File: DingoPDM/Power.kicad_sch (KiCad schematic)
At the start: 29 parts, among them J5 SHORT, SW2 AlwaysOn, U18 LD1117S33CTR, U22 VXO780x-500-M, U23 ISP752R

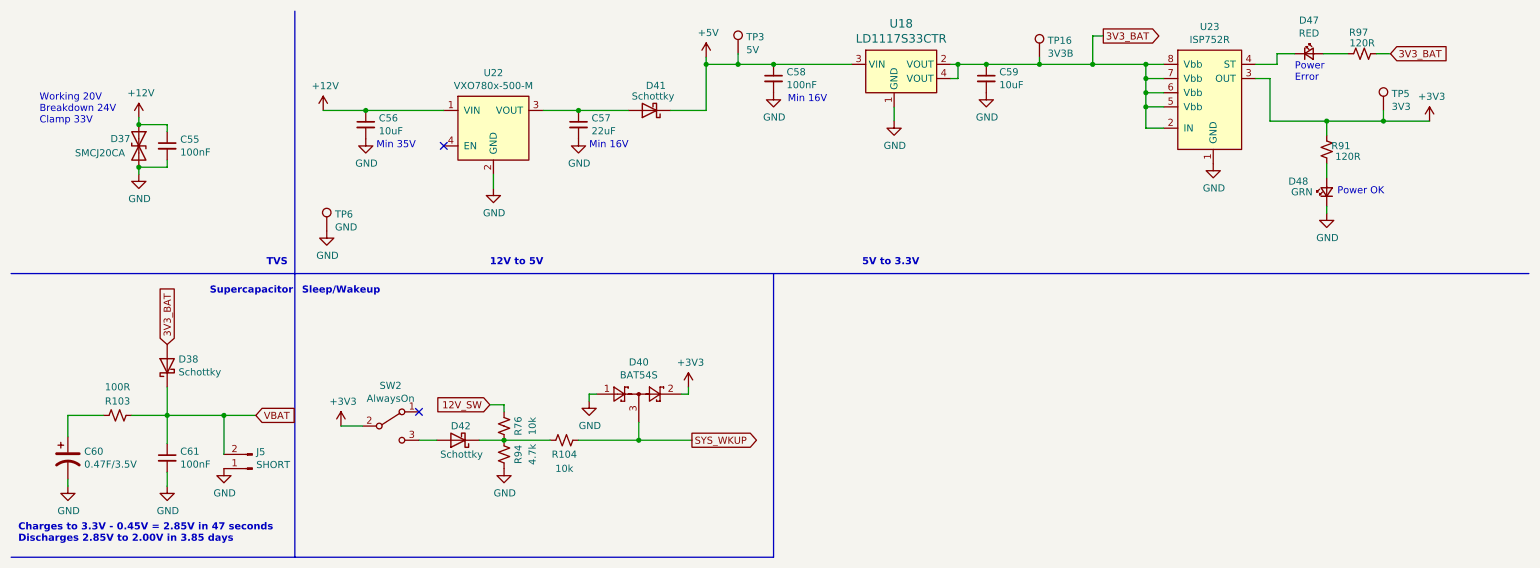
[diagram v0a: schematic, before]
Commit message: Swapped to AMPSEAL 14 pins
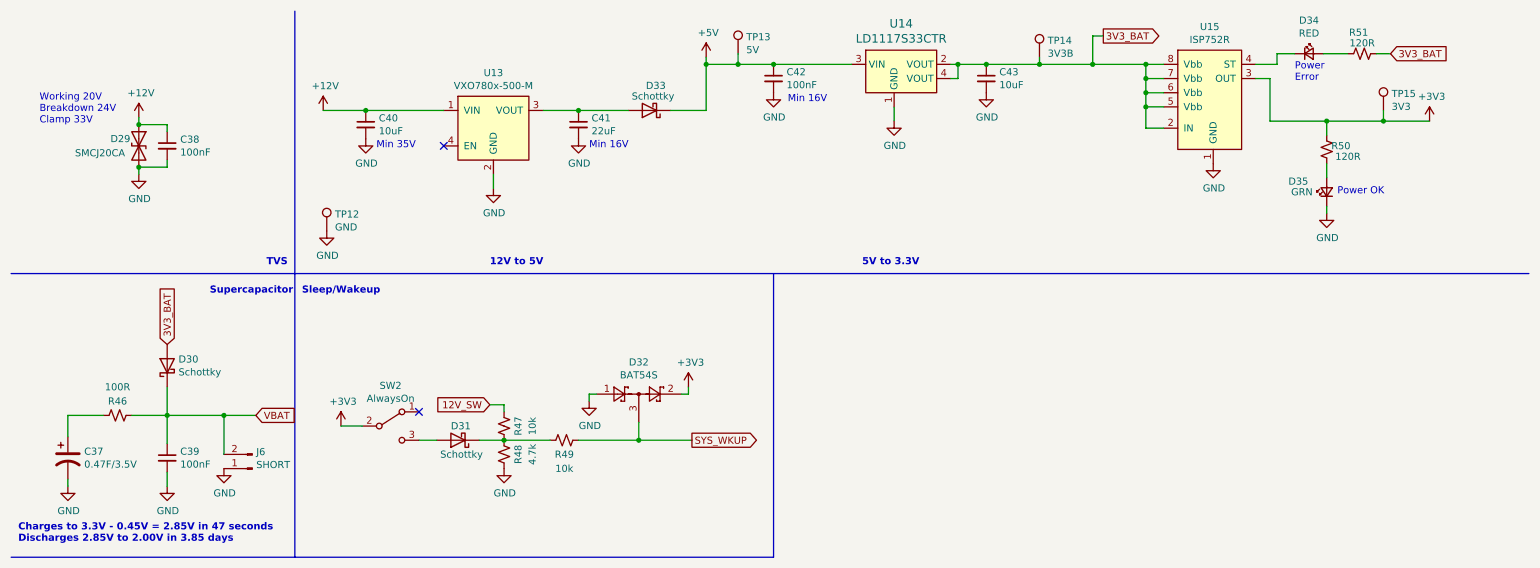
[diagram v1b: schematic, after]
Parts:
- renumbered C60 to C37, C55 to C38, C61 to C39, C56 to C40, C57 to C41, C58 to C42, C59 to C43, D37 to D29, D38 to D30, D42 to D31, D40 to D32, D41 to D33, D47 to D34, D48 to D35, J5 to J6, R103 to R46, R76 to R47, R94 to R48, R104 to R49, R91 to R50, R97 to R51, TP6 to TP12, TP3 to TP13, TP16 to TP14, TP5 to TP15, U22 to U13, U18 to U14, U23 to U15

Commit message: Removed unused IRQs, added pd res on PF GPIO reset
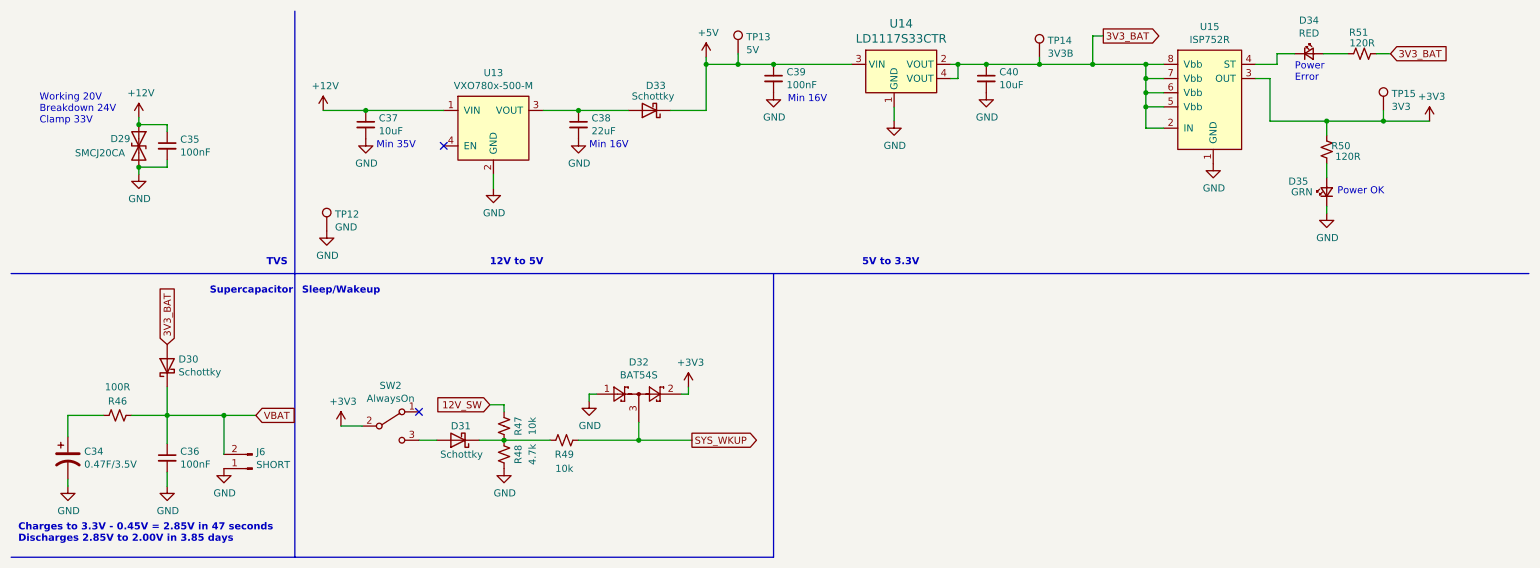
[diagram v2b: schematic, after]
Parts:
- renumbered C37 to C34, C38 to C35, C39 to C36, C40 to C37, C41 to C38, C42 to C39, C43 to C40
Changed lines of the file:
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@@
   (symbol (lib_id "power:+12V") (at 68.58 31.75 0) (unit 1)
     (in_bom yes) (on_board yes)
-    (property "Reference" "#PWR0123" (id 0) (at 68.58 35.56 0)
+    (property "Reference" "#PWR0120" (id 0) (at 68.58 35.56 0)
       (effects (font (size 1.27 1.27)) hide)
     )
@@
   (symbol (lib_id "power:GND") (at 99.06 45.72 0) (unit 1)
     (in_bom yes) (on_board yes)
-    (property "Reference" "#PWR0127" (id 0) (at 99.06 52.07 0)
+    (property "Reference" "#PWR0124" (id 0) (at 99.06 52.07 0)
       (effects (font (size 1.27 1.27)) hide)
     )
@@
   (symbol (lib_id "power:GND") (at 35.56 43.18 0) (unit 1)
     (in_bom yes) (on_board yes)
-    (property "Reference" "#PWR0120" (id 0) (at 35.56 49.53 0)
+    (property "Reference" "#PWR0117" (id 0) (at 35.56 49.53 0)
       (effects (font (size 1.27 1.27)) hide)
     )
@@
   (symbol (lib_id "power:+12V") (at 35.56 33.02 0) (unit 1)
     (in_bom yes) (on_board yes)
-    (property "Reference" "#PWR0119" (id 0) (at 35.56 36.83 0)
+    (property "Reference" "#PWR0116" (id 0) (at 35.56 36.83 0)
       (effects (font (size 1.27 1.27)) hide)
     )
@@
   (symbol (lib_id "Device:C_Small") (at 40.64 38.1 0) (unit 1)
     (in_bom yes) (on_board yes)
-    (property "Reference" "C38" (id 0) (at 42.9768 36.9316 0)
+    (property "Reference" "C35" (id 0) (at 42.9768 36.9316 0)
       (effects (font (size 1.27 1.27)) (justify left))
     )
@@
   (symbol (lib_id "Device:C_Small") (at 76.2 34.29 0) (unit 1)
     (in_bom yes) (on_board yes)
-    (property "Reference" "C40" (id 0) (at 78.5368 33.1216 0)
+    (property "Reference" "C37" (id 0) (at 78.5368 33.1216 0)
       (effects (font (size 1.27 1.27)) (justify left))
     )
@@
   (symbol (lib_id "Device:C_Small") (at 114.3 34.29 0) (unit 1)
     (in_bom yes) (on_board yes)
-    (property "Reference" "C41" (id 0) (at 116.6368 33.1216 0)
+    (property "Reference" "C38" (id 0) (at 116.6368 33.1216 0)
       (effects (font (size 1.27 1.27)) (justify left))
     )
@@
   (symbol (lib_id "power:GND") (at 114.3 36.83 0) (unit 1)
     (in_bom yes) (on_board yes)
-    (property "Reference" "#PWR0129" (id 0) (at 114.3 43.18 0)
+    (property "Reference" "#PWR0126" (id 0) (at 114.3 43.18 0)
       (effects (font (size 1.27 1.27)) hide)
     )
@@
   (symbol (lib_id "power:GND") (at 76.2 36.83 0) (unit 1)
     (in_bom yes) (on_board yes)
-    (property "Reference" "#PWR0126" (id 0) (at 76.2 43.18 0)
+    (property "Reference" "#PWR0123" (id 0) (at 76.2 43.18 0)
       (effects (font (size 1.27 1.27)) hide)
     )
@@
   (symbol (lib_id "Device:C_Small") (at 149.225 26.035 0) (unit 1)
     (in_bom yes) (on_board yes)
-    (property "Reference" "C42" (id 0) (at 151.5618 24.8666 0)
+    (property "Reference" "C39" (id 0) (at 151.5618 24.8666 0)
       (effects (font (size 1.27 1.27)) (justify left))
     )
@@
   (symbol (lib_id "power:+3V3") (at 266.7 33.655 0) (unit 1)
     (in_bom yes) (on_board yes)
-    (property "Reference" "#PWR0138" (id 0) (at 266.7 37.465 0)
+    (property "Reference" "#PWR0135" (id 0) (at 266.7 37.465 0)
       (effects (font (size 1.27 1.27)) hide)
     )
@@
   (symbol (lib_id "power:GND") (at 100.965 95.885 0) (unit 1)
     (in_bom yes) (on_board yes)
-    (property "Reference" "#PWR0128" (id 0) (at 100.965 102.235 0)
+    (property "Reference" "#PWR0125" (id 0) (at 100.965 102.235 0)
       (effects (font (size 1.27 1.27)) hide)
     )
@@
   (symbol (lib_id "Device:C_Small") (at 187.325 26.035 0) (unit 1)
     (in_bom yes) (on_board yes)
-    (property "Reference" "C43" (id 0) (at 189.6618 24.8666 0)
+    (property "Reference" "C40" (id 0) (at 189.6618 24.8666 0)
       (effects (font (size 1.27 1.27)) (justify left))
     )
@@
   (symbol (lib_id "power:GND") (at 170.815 33.655 0) (unit 1)
     (in_bom yes) (on_board yes)
-    (property "Reference" "#PWR0134" (id 0) (at 170.815 40.005 0)
+    (property "Reference" "#PWR0131" (id 0) (at 170.815 40.005 0)
       (effects (font (size 1.27 1.27)) hide)
     )
@@
   (symbol (lib_id "power:GND") (at 149.225 28.575 0) (unit 1)
     (in_bom yes) (on_board yes)
-    (property "Reference" "#PWR0133" (id 0) (at 149.225 34.925 0)
+    (property "Reference" "#PWR0130" (id 0) (at 149.225 34.925 0)
       (effects (font (size 1.27 1.27)) hide)
     )
@@
   (symbol (lib_id "power:GND") (at 187.325 28.575 0) (unit 1)
     (in_bom yes) (on_board yes)
-    (property "Reference" "#PWR0135" (id 0) (at 187.325 34.925 0)
+    (property "Reference" "#PWR0132" (id 0) (at 187.325 34.925 0)
       (effects (font (size 1.27 1.27)) hide)
     )
@@
   (symbol (lib_id "power:GND") (at 116.205 83.82 0) (unit 1)
     (in_bom yes) (on_board yes)
-    (property "Reference" "#PWR0130" (id 0) (at 116.205 90.17 0)
+    (property "Reference" "#PWR0127" (id 0) (at 116.205 90.17 0)
       (effects (font (size 1.27 1.27)) hide)
     )
@@
   (symbol (lib_id "Device:CP1") (at 22.86 93.98 0) (unit 1)
     (in_bom yes) (on_board yes)
-    (property "Reference" "C37" (id 0) (at 25.781 92.8116 0)
+    (property "Reference" "C34" (id 0) (at 25.781 92.8116 0)
       (effects (font (size 1.27 1.27)) (justify left))
     )
@@
   (symbol (lib_id "Device:C_Small") (at 40.64 93.98 0) (unit 1)
     (in_bom yes) (on_board yes)
-    (property "Reference" "C39" (id 0) (at 42.9768 92.8116 0)
+    (property "Reference" "C36" (id 0) (at 42.9768 92.8116 0)
       (effects (font (size 1.27 1.27)) (justify left))
     )
@@
   (symbol (lib_id "power:GND") (at 69.215 53.34 0) (unit 1)
     (in_bom yes) (on_board yes)
-    (property "Reference" "#PWR0124" (id 0) (at 69.215 59.69 0)
+    (property "Reference" "#PWR0121" (id 0) (at 69.215 59.69 0)
       (effects (font (size 1.27 1.27)) hide)
     )
@@
   (symbol (lib_id "power:GND") (at 40.64 99.06 0) (unit 1)
     (in_bom yes) (on_board yes)
-    (property "Reference" "#PWR0121" (id 0) (at 40.64 105.41 0)
+    (property "Reference" "#PWR0118" (id 0) (at 40.64 105.41 0)
       (effects (font (size 1.27 1.27)) hide)
     )
@@
   (symbol (lib_id "power:GND") (at 22.86 99.06 0) (unit 1)
     (in_bom yes) (on_board yes)
-    (property "Reference" "#PWR0118" (id 0) (at 22.86 105.41 0)
+    (property "Reference" "#PWR0115" (id 0) (at 22.86 105.41 0)
       (effects (font (size 1.27 1.27)) hide)
     )
@@
   (symbol (lib_id "power:+5V") (at 137.16 22.225 0) (unit 1)
     (in_bom yes) (on_board yes)
-    (property "Reference" "#PWR0132" (id 0) (at 137.16 26.035 0)
+    (property "Reference" "#PWR0129" (id 0) (at 137.16 26.035 0)
       (effects (font (size 1.27 1.27)) hide)
     )
@@
   (symbol (lib_id "power:GND") (at 50.8 95.885 0) (unit 1)
     (in_bom yes) (on_board yes)
-    (property "Reference" "#PWR0122" (id 0) (at 50.8 102.235 0)
+    (property "Reference" "#PWR0119" (id 0) (at 50.8 102.235 0)
       (effects (font (size 1.27 1.27)) hide)
     )
@@
   (symbol (lib_id "power:+3V3") (at 71.755 88.265 0) (unit 1)
     (in_bom yes) (on_board yes)
-    (property "Reference" "#PWR0125" (id 0) (at 71.755 92.075 0)
+    (property "Reference" "#PWR0122" (id 0) (at 71.755 92.075 0)
       (effects (font (size 1.27 1.27)) hide)
     )
@@
   (symbol (lib_id "power:+3V3") (at 133.985 81.28 0) (unit 1)
     (in_bom yes) (on_board yes)
-    (property "Reference" "#PWR0131" (id 0) (at 133.985 85.09 0)
+    (property "Reference" "#PWR0128" (id 0) (at 133.985 85.09 0)
       (effects (font (size 1.27 1.27)) hide)
     )
@@
   (symbol (lib_id "power:GND") (at 227.965 41.275 0) (unit 1)
     (in_bom yes) (on_board yes)
-    (property "Reference" "#PWR0136" (id 0) (at 227.965 47.625 0)
+    (property "Reference" "#PWR0133" (id 0) (at 227.965 47.625 0)
       (effects (font (size 1.27 1.27)) hide)
     )
@@
   (symbol (lib_id "power:GND") (at 248.285 50.165 0) (unit 1)
     (in_bom yes) (on_board yes)
-    (property "Reference" "#PWR0137" (id 0) (at 248.285 56.515 0)
-      (effects (font (size 1.27 1.27)) hide)
-    )
+    (property "Reference" "#PWR0134" (id 0) (at 248.285 56.515 0)
+      (effects (font (size 1.27 1.27)) hide)
+    )

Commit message: layout finished
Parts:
- removed D32: BAT54S, Package_TO_SOT_SMD:SOT-23, symbol Diode:BAT54S
- removed R47: 10k, Resistor_SMD:R_0805_2012Metric, symbol Device:R_Small_US
- added C39: 100nF, Capacitor_SMD:C_0805_2012Metric, symbol Device:C_Small
- added U14: TLP2361_TPL_E, Profet:TLP2710(TP,E, symbol dk_Optoisolators-Logic-Output:TLP2361_TPL_E
- R47: renamed from R48; value 4.7k -> 470R
- renumbered C39 to C40, C40 to C41, D33 to D32, D34 to D33, D35 to D34, R49 to R48, R50 to R49, R51 to R50, U14 to U15, U15 to U16
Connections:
- net +3V3: now also R47.2, C39.1, U14.6 (VCC); no longer SW2.2 (B)
- net GND: now also SW2.2 (B), C39.2, U14.4 (GND); no longer R47.1
- net at D31.2 (A), SW2.3 (C): now also U14.3
- new net: R47.1, U14.1
- new net: R48.1, U14.5 (VO)
- new net ON_SW: D31.1 (K)
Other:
- moved on the sheet: D31, R47, R48, SW2

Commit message: Added export, fixed some PNs
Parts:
- D33: Digi-Key_PN 475-2560-1-ND -> 475-1278-1-ND
- D34: Digi-Key_PN 475-2560-1-ND -> 475-1410-1-ND
- U16: Digi-Key_PN (none) -> ISP752RFUMA1CT-ND

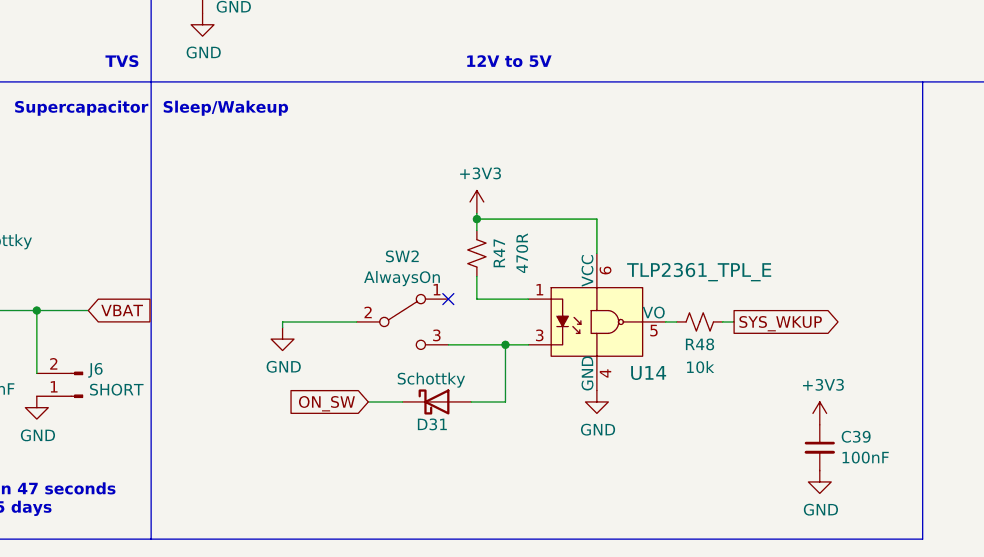
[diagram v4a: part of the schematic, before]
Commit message: V5 changes
Changed tracks/clearances/DRC to meet JLCPCB 2oz rules. Changed on switch to 12V input. Switched to TagConnect
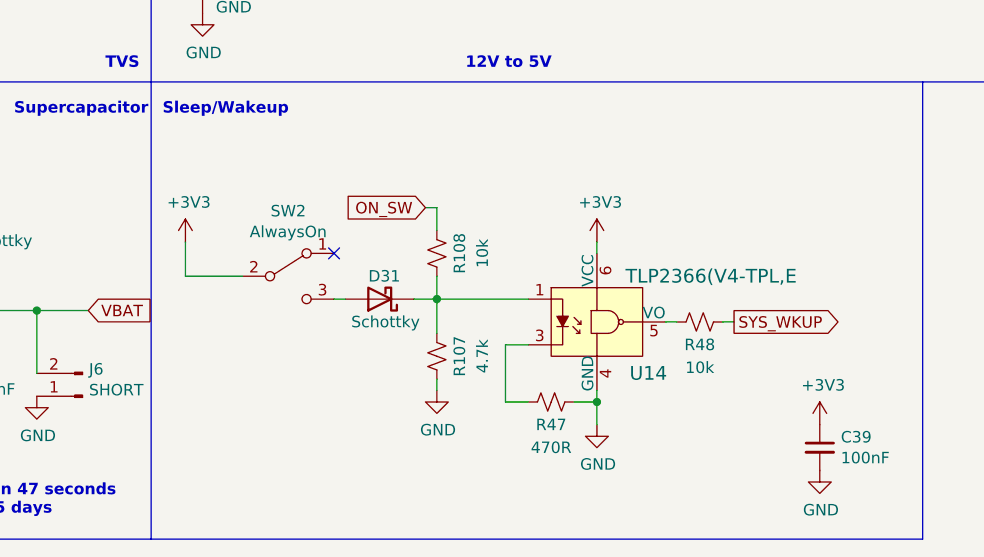
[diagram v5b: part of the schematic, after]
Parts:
- added R107: 4.7k, Resistor_SMD:R_0805_2012Metric, symbol Device:R_Small_US
- added R108: 10k, Resistor_SMD:R_0805_2012Metric, symbol Device:R_Small_US
- U14: value TLP2361_TPL_E -> TLP2366(V4-TPL,E; DK_Datasheet_Link https://toshiba.semicon-storage.com/info/docget.jsp?did=142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 -> (none); DK_Detail_Page /product-detail/en/toshiba-semiconductor-and-storage/TLP236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 -> (none); Digi-Key_PN TLP2361(TPLECT-ND -> TLP2366(V4-TPLECT-ND; Family Optoisolators - Logic Output -> (none); MPN TLP2361(TPL,E -> TLP2366(V4-TPL,E; Manufacturer Toshiba Semiconductor and Storage -> (none); Status Active -> (none)
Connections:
- net +3V3: now also SW2.2 (B); no longer R47.2
- net GND: now also R47.2, R107.1; no longer SW2.2 (B)
- net ON_SW: now also R108.2; no longer D31.1 (K)
- net at R47.1: now also U14.3; no longer U14.1
- net at D31.2 (A), SW2.3 (C): no longer U14.3
- new net: D31.1 (K), R107.2, R108.1, U14.1
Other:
- moved on the sheet: D31, R47, SW2
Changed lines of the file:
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@@
-(kicad_sch (version 20211123) (generator eeschema)
+(kicad_sch (version 20230121) (generator eeschema)
   (paper "A4")

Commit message: Documentation cleanup
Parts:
- C34: PN FC0V474ZFTBR24 -> (none)
- R108: Digi-Key_PN 311-4.70KCRCT-ND -> 311-10.0KCRDKR-ND
- U14: Category Isolators -> (none); MPN TLP2366(V4-TPL,E -> (none)
- U15: Category Integrated Circuits (ICs) -> (none); DK_Datasheet_Link http://www.st.com/content/ccc/resource/technical/document/d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 -> (none); DK_Detail_Page /product-detail/en/stmicroelectronics/LD1117S33CTR/497-1241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 -> (none); Family PMIC - Voltage Regulators - Linear -> (none); MPN LD1117S33CTR -> (none); Manufacturer STMicroelectronics -> (none); Status Active -> (none)

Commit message: V5 As Built
-Changed ADS1015 to MAX11613EUA+T due to supply issues
-Changed PCB to match JLCPCB 2oz rules
-Changed ON_SW input to 12V switched
-Switched to TagConnect TC2030
-Changed pin positions of GND, IN1, IN2
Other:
- title: (none) -> Dingo_PDM
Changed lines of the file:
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@@
 (kicad_sch (version 20230121) (generator eeschema)
   (paper "A4")
+  (title_block
+    (title "Dingo_PDM")
+    (date "2023-02-23")
+    (rev "v5")
+    (comment 3 "github.com/corygrant")
+    (comment 4 "Cory Grant")
+  )

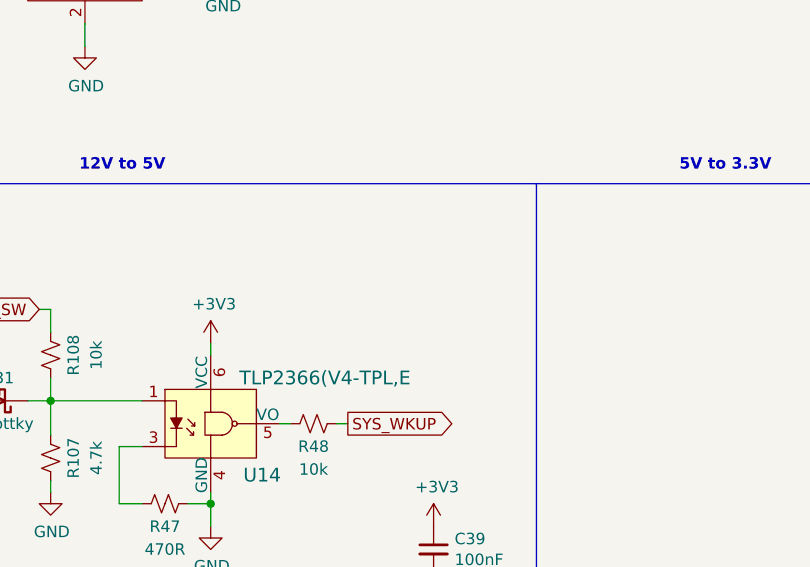
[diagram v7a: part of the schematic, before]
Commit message: Incorrect PN for some diodes and resistors
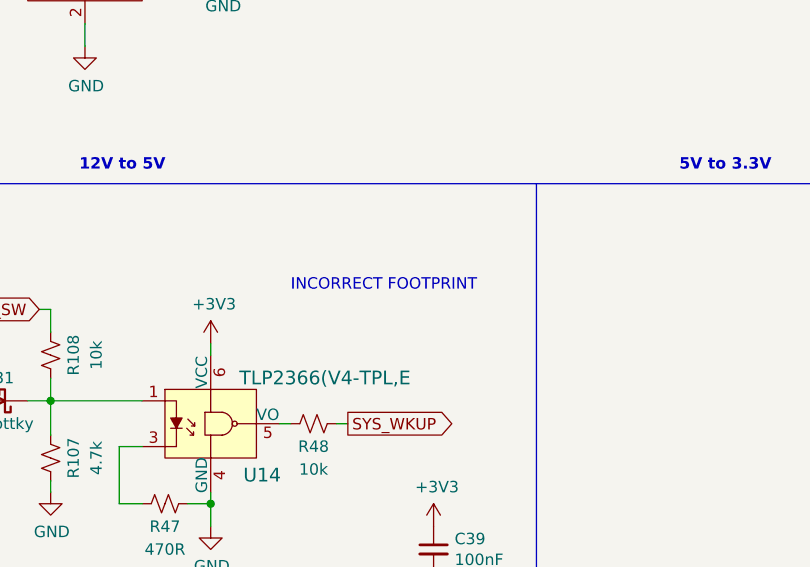
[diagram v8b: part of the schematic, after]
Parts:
- R47: Digi-Key_PN 311-4.70KCRCT-ND -> 311-470CRCT-ND
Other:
- note added: "INCORRECT FOOTPRINT"
